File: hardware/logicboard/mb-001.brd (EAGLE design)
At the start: 91 x 57 mm, 11 parts, among them J1 DIN5, J2 DIN5, J3 DIN5, J4 AUDIO_JACK_3.5MM_KIT, J5 AUDIO_JACK_3.5MM_KIT, J6 AUDIO_JACK_3.5MM_KIT

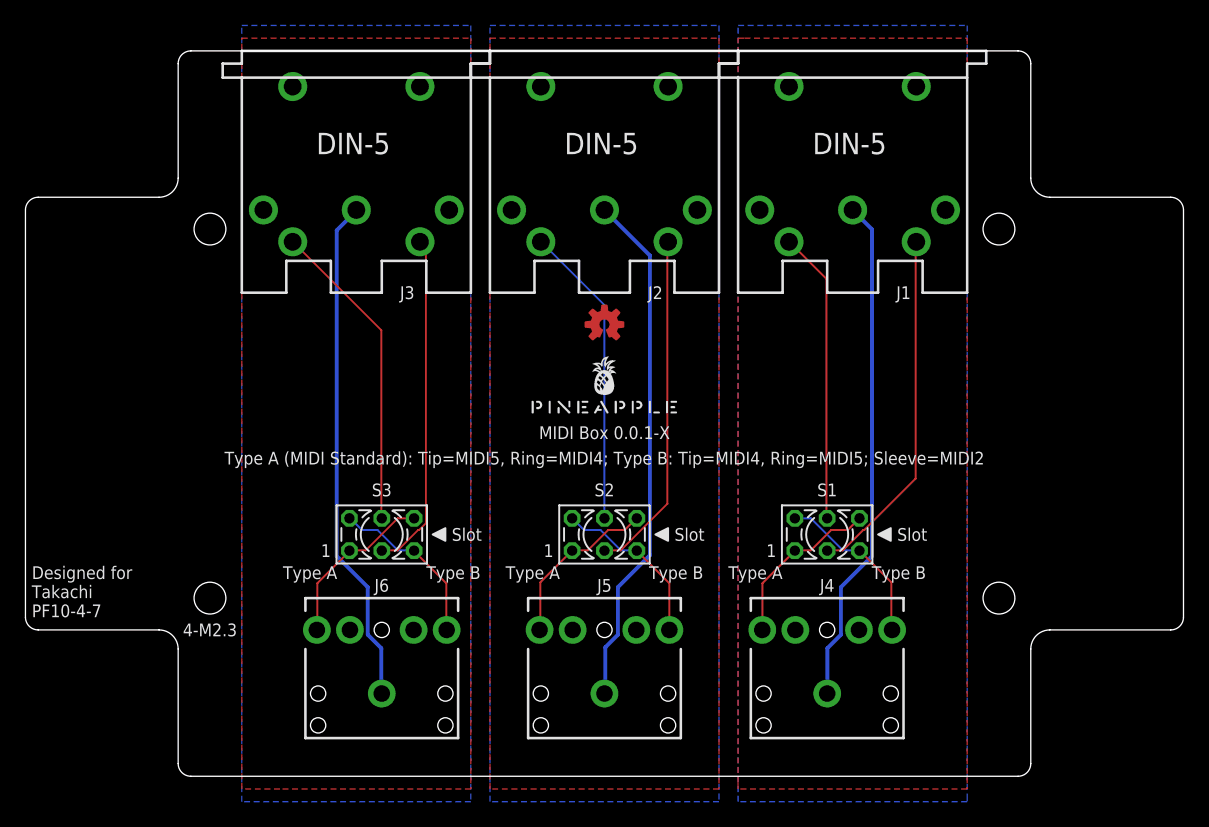
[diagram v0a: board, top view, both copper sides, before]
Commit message: Align of TRS jacks.
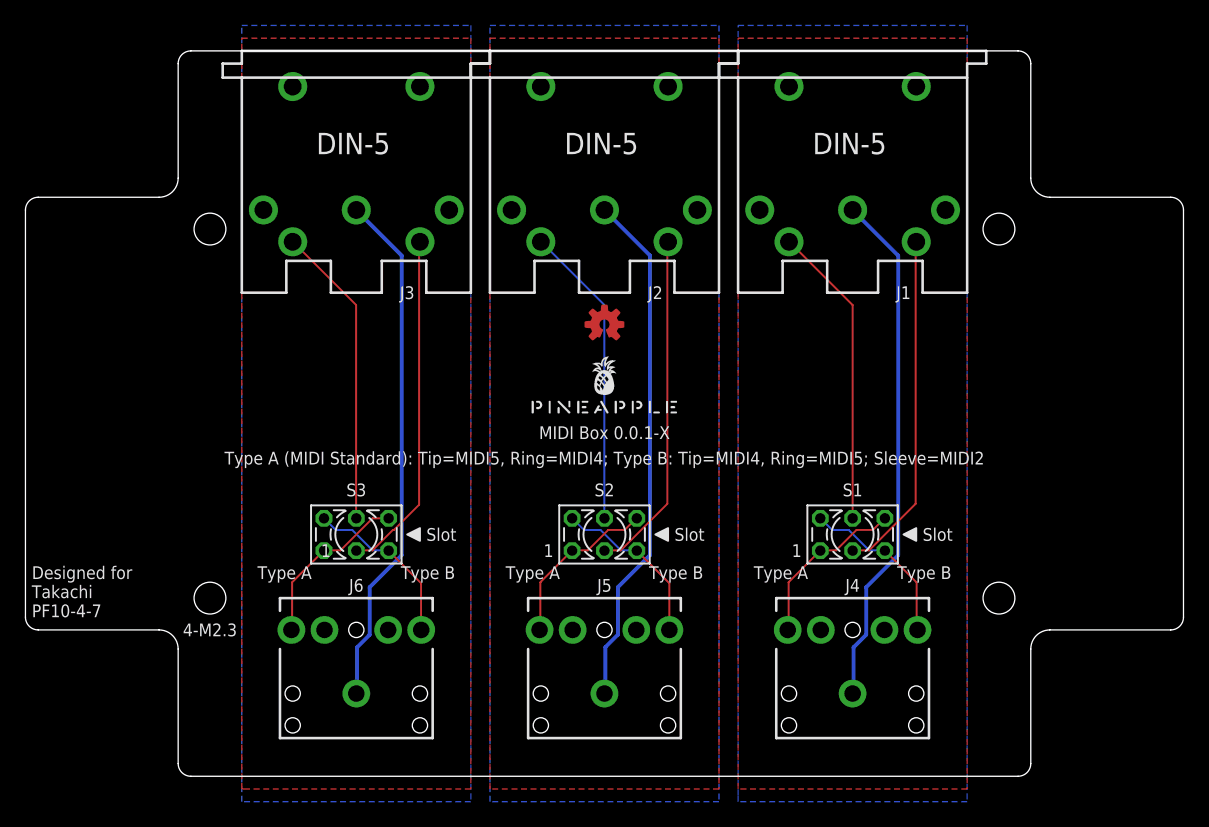
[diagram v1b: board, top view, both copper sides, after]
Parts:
- moved J4 2.00 mm to (65.0, 6.50)
- moved J6 2.00 mm to (26.0, 6.50)
- moved S1 2.00 mm to (65.0, 19.0)
- moved S3 2.00 mm to (26.0, 19.0)
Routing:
- net M1GND: track 40.1 -> 41.0 mm
- net M3GND: track 40.1 -> 41.0 mm
- net M1RTN: track 27.9 -> 27.1 mm
- net M1SND: track 23.0 -> 23.8 mm
- net M3SND: track 24.6 -> 23.8 mm
